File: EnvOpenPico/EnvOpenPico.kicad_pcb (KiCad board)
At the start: 2 copper layers, 21.5 x 51.3 mm, 57 parts, among them J2 SKRKAEE020, J3 2.54mm header 01x20, J4 2.54mm header 01x20, J5 Conn_01x03_Male, U1 TLV75533PDBVR, U3 RP2040, Y1 3225_4P

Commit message: dont remember what I changed but commit for safety
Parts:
- removed kibuzzard-628ADE15: G***, kibuzzard-628ADE15

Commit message: updated readme
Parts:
- removed kibuzzard-628939D8: G***, kibuzzard-628939D8
- removed kibuzzard-628939E9: G***, kibuzzard-628939E9
- removed kibuzzard-62893A77: G***, kibuzzard-62893A77
- removed kibuzzard-628A86BE: G***, kibuzzard-628A86BE
- FLASH1: value ZD25WQ16BUIGR -> w25q16jvuxiq
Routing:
- net GND: track 33.5 -> 31.8 mm
- net /RUN: track 14.1 -> 15.0 mm

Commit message: faff and things, no important changes.
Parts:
- removed kibuzzard-628A892C: G***, kibuzzard-628A892C
- FLASH1: value w25q16jvuxiq -> W25Q16JV
- U1: value TLV75533PDBVR -> TLV75733PDBVR
- moved C15 1.41 mm to (98.2, 80.2), turned to 90 degrees
- moved R1 1.02 mm to (100.6, 75.0)
- moved R2 0.88 mm to (98.8, 75.1)
- moved C5 0.38 mm to (98.8, 76.1)
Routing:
- net GND: track 31.8 -> 33.8 mm
- net /~{USB_BOOT}: track 5.99 -> 4.95 mm
- net /RUN: track 15.0 -> 14.4 mm
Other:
- board text added: "BOOT"

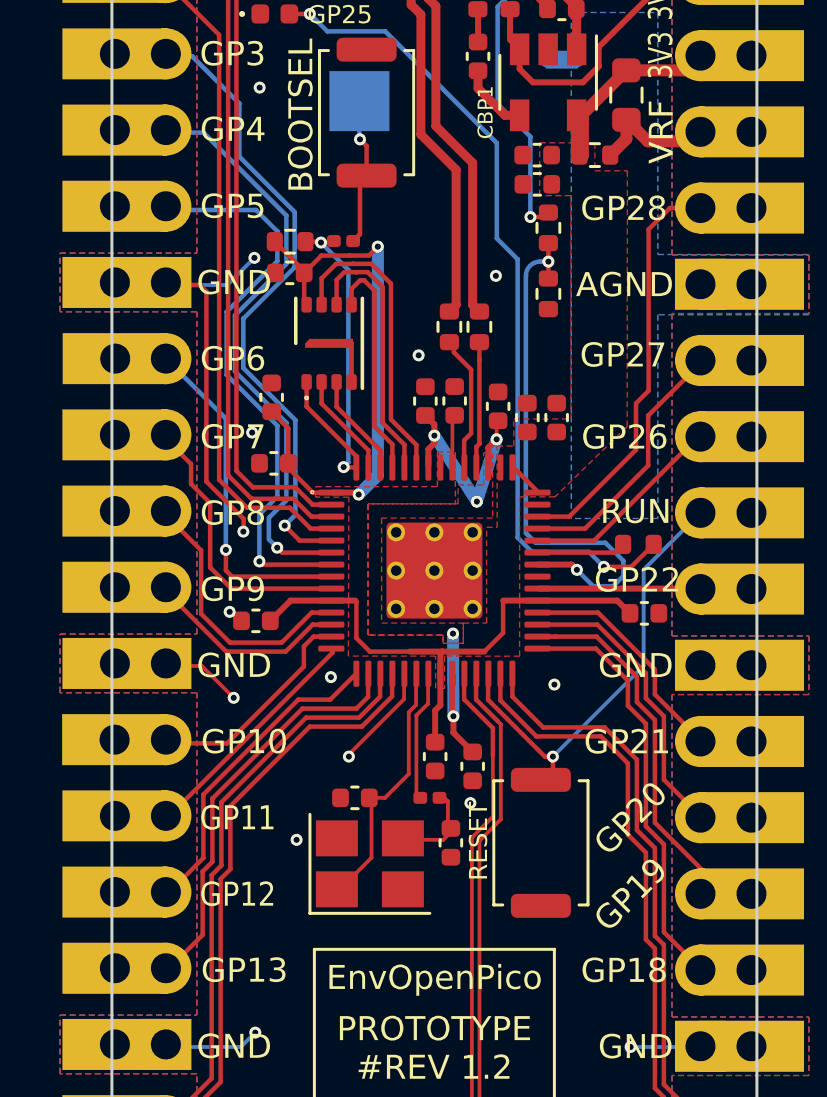
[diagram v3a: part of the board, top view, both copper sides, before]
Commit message: lots of changes, swapped many parts to 0402, swapped SOT regulator to small WSON, made sure there is proper parity between footprint and value, etc etc etc
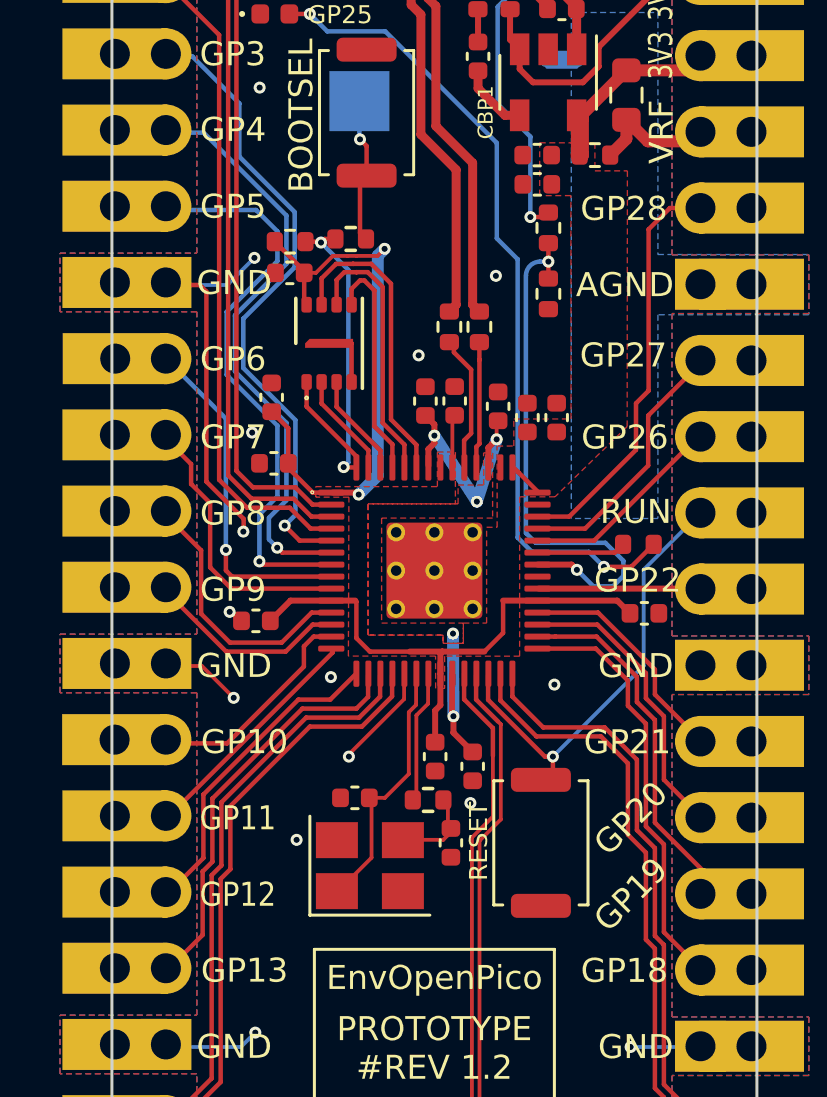
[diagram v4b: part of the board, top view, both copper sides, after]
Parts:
- R1, R11: value 1K 0201 -> 1K 0402; footprint Resistor_SMD:R_0201_0603Metric -> Resistor_SMD:R_0402_1005Metric
- moved R1 0.25 mm to (100.9, 75.0)
- moved R11 0.09 mm to (103.4, 93.7)
- moved Y1 0.06 mm to (101.5, 95.9)

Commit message: made some smaller components generated new gerber
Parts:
- J2, RSW1: value SKRKAEE020 -> TSA343G00-250J2
- moved RSW1 0.66 mm to (107.1, 95.8)
- moved C16 0.57 mm to (107.9, 80.4)
- moved C10 0.55 mm to (106.8, 80.4)
- moved C3 0.17 mm to (105.8, 80.4)
- moved GPIO25_LED1 0.16 mm to (98.3, 67.3)
- moved J2 0.12 mm to (101.5, 70.7)
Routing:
- net /RUN: track 14.4 -> 15.8 mm
- net /~{USB_BOOT}: track 4.87 -> 5.92 mm
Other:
- board text added: "25"
- board text removed: "GP25"

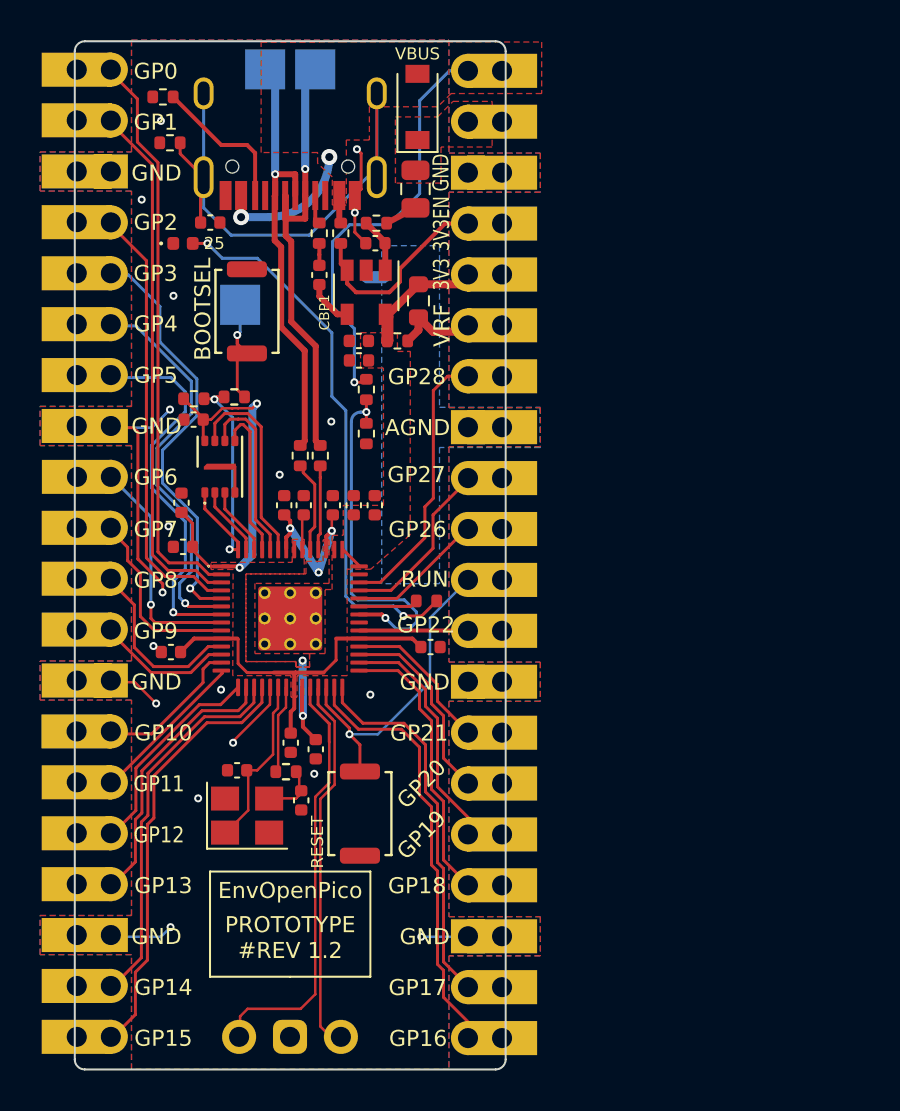
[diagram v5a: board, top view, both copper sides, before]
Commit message: swapped flash for one that was in stock.
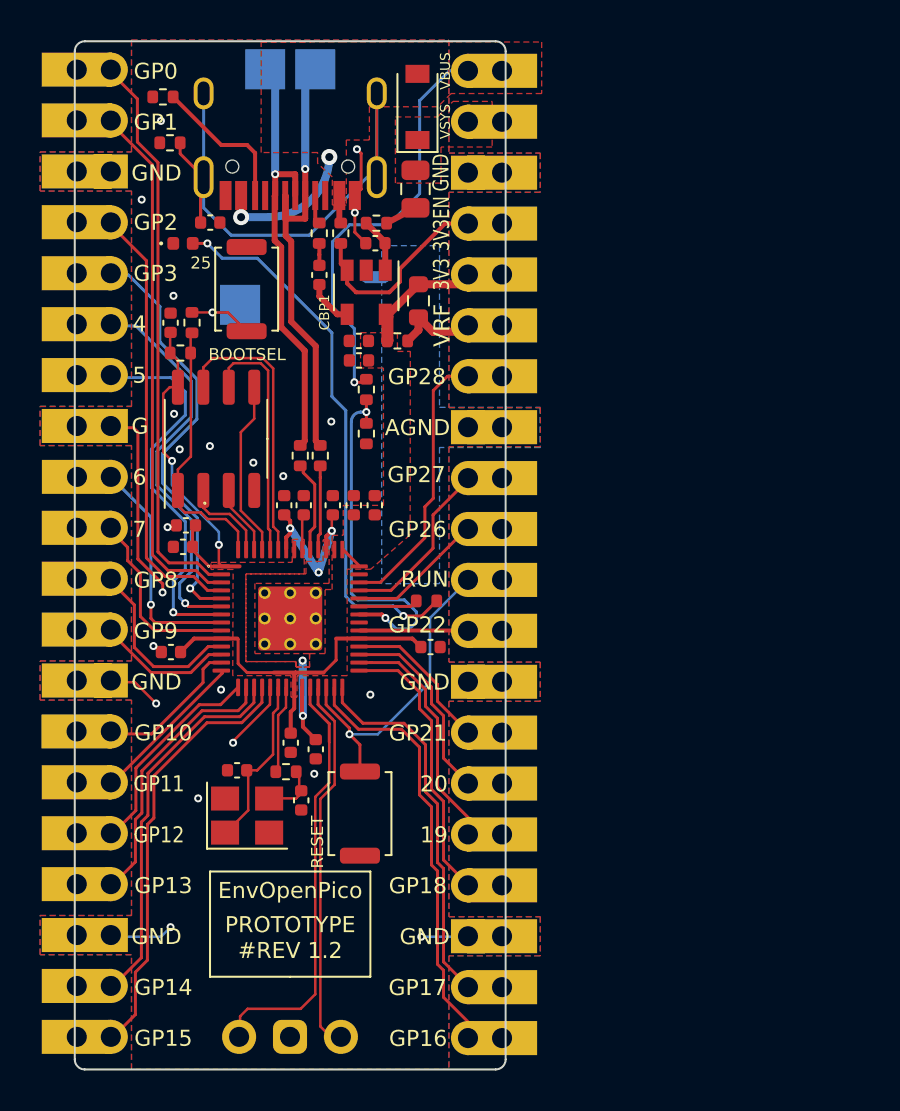
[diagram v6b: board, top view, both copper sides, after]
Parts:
- FLASH1: value W25Q16JV -> W25Q16JVSNIQ; footprint Package_SON:SON-8-1EP_3x2mm_P0.5mm_EP1.4x1.6mm -> Package_SO:SO-8_3.9x4.9mm_P1.27mm
- moved C5 4.97 mm to (97.7, 71.3), turned to 90 degrees
- moved R1 4.27 mm to (98.7, 71.3), turned to 90 degrees
- moved R2 2.38 mm to (98.2, 72.8)
- moved FLASH1 1.40 mm to (100.0, 77.1)
- moved C15 1.15 mm to (98.4, 81.4), turned to 180 degrees
- moved J2 1.11 mm to (101.5, 69.6)
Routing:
- net GND: track 33.8 -> 28.5 mm, vias 19 -> 22
- net /QSPI_SD3: track 10.1 -> 14.0 mm
- net /QSPI_SCLK: track 8.99 -> 12.1 mm
- net +3V3: track 47.0 -> 45.7 mm
- net /~{USB_BOOT}: track 5.92 -> 4.65 mm
- net /QSPI_SD0: track 7.69 -> 8.82 mm
- net /QSPI_SD1: track 3.50 -> 4.42 mm
- net /QSPI_SS: track 12.9 -> 13.4 mm, vias 2 -> 0
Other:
- board text added: "19"
- board text added: "20"
- board text added: "4"
- board text added: "5"
- board text added: "6"
- board text added: "7"
- board text added: "G"

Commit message: various updates including README
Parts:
- R3, R4: value 27 0402 -> 27r 0402 resistor
- U1: value TLV75733PDBVR -> SOT-23-5 5.5V 3.3V 500mA
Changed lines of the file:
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@@
       (effects (font (size 1 1) (thickness 0.15)))
     )
-    (fp_text value "27 0402" (at 0 1.17 90) (layer "F.Fab")
+    (fp_text value "27r 0402 resistor" (at 0 1.17 90) (layer "F.Fab")
       (effects (font (size 1 1) (thickness 0.15)))
     )
@@
       (effects (font (size 1 1) (thickness 0.15)))
     )
-    (fp_text value "27 0402" (at 0 1.17 90) (layer "F.Fab")
+    (fp_text value "27r 0402 resistor" (at 0 1.17 90) (layer "F.Fab")
       (effects (font (size 1 1) (thickness 0.15)))
     )
@@
       (effects (font (size 1 1) (thickness 0.15)))
     )
-    (fp_text value "TLV75733PDBVR" (at 0 2.9 90) (layer "F.Fab")
-      (effects (font (size 1 1) (thickness 0.15)))
-    )
+    (fp_text value "SOT-23-5 5.5V 3.3V 500mA" (at 0 2.9 90) (layer "F.Fab")
+      (effects (font (size 1 1) (thickness 0.15)))
+    )

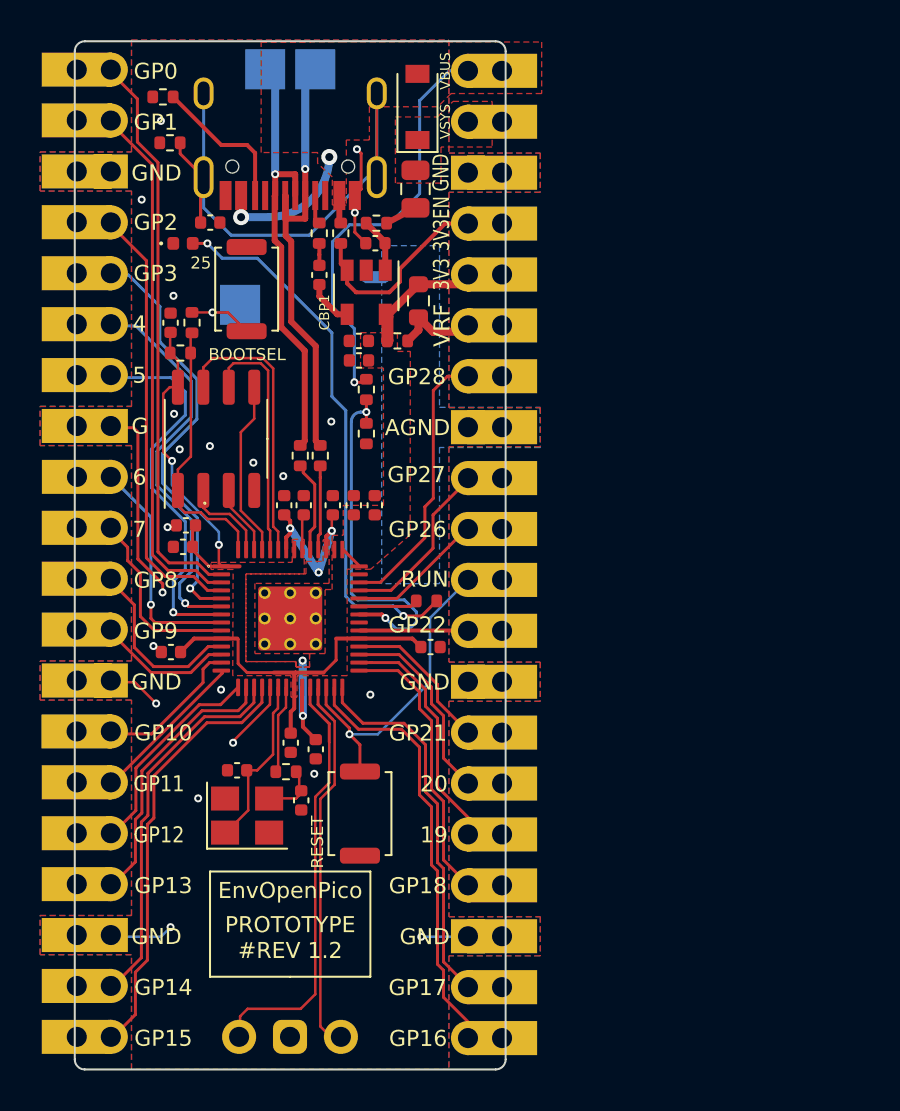
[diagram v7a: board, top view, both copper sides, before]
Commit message: incr version, added mosfet and led for GP23, marked GP24, tiny bits of cleanup and DRC checks.
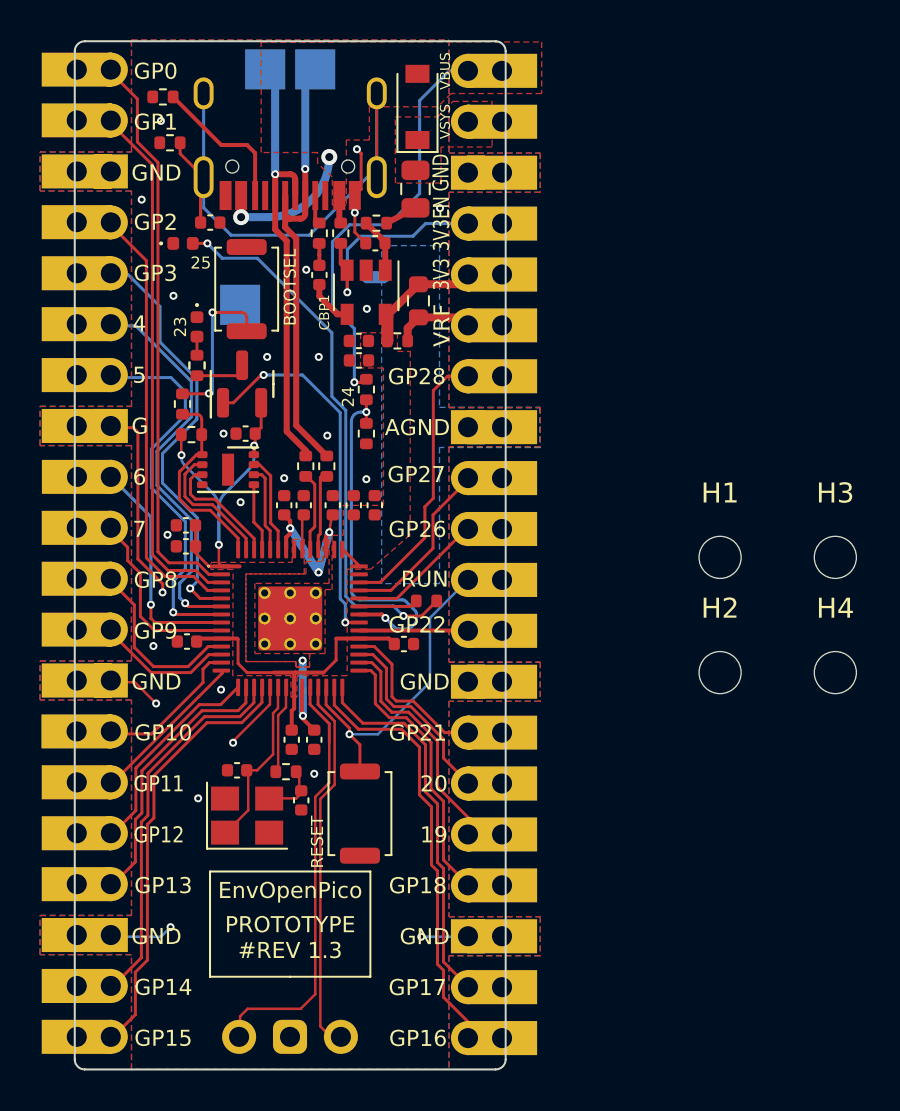
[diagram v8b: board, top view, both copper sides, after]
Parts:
- added GP23_LED1: GP23 LED_0402, LED_SMD:LED_0402_1005Metric, F.Cu at (99.0, 71.5)
- added GPIO24_RESISTOR1: 1K 0402, Resistor_SMD:R_0402_1005Metric, F.Cu at (99.0, 73.4)
- added H1: MountingHole, MountingHole:MountingHole_2.1mm, F.Cu at (125.1, 83.0)
- added H2: MountingHole, MountingHole:MountingHole_2.1mm, F.Cu at (125.1, 88.7)
- added H3: MountingHole, MountingHole:MountingHole_2.1mm, F.Cu at (130.8, 83.0)
- added H4: MountingHole, MountingHole:MountingHole_2.1mm, F.Cu at (130.8, 88.7)
- added Q1: SI2301B, Package_TO_SOT_SMD:SOT-23, F.Cu at (101.2, 74.3)
- FLASH1: value W25Q16JVSNIQ -> W25Q16JVUXIQ; footprint Package_SO:SO-8_3.9x4.9mm_P1.27mm -> Package_SON:SON-8-1EP_3x2mm_P0.5mm_EP1.4x1.6mm
- R102: value 1M 0402 -> 220 0402
- moved C5 6.68 mm to (101.4, 76.8), turned to 180 degrees
- moved R2 4.11 mm to (98.7, 76.8)
- moved R1 4.09 mm to (98.3, 75.3)
- moved FLASH1 1.65 mm to (100.5, 78.6), turned to 0 degrees
- moved C13 1.33 mm to (109.3, 87.3)
- moved C18 0.96 mm to (98.5, 87.2)
- moved R4 0.62 mm to (105.5, 78.4)
- moved R3 0.59 mm to (104.4, 78.4)
- moved C6 0.48 mm to (104.8, 92.1)
- moved C14 0.16 mm to (103.7, 92.1)
- moved C11 0.15 mm to (98.5, 82.4)
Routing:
- net /GPIO23: track 0.00 -> 18.5 mm, vias 0 -> 2
- net /QSPI_SD3: track 14.0 -> 4.96 mm
- net /QSPI_SCLK: track 12.1 -> 4.30 mm
- net /QSPI_SD0: track 8.82 -> 3.41 mm
- net /~{USB_BOOT}: track 4.65 -> 9.61 mm, vias 1 -> 2
- net /QSPI_SS: track 13.4 -> 10.0 mm
- net Net-(GPIO24_RESISTOR1-Pad2): track 0.00 -> 2.77 mm
- net /QSPI_SD2: track 3.48 -> 6.07 mm
- net /QSPI_SD1: track 4.42 -> 6.66 mm
- net 3V3_EN: track 9.67 -> 11.3 mm, vias 0 -> 1
- net Net-(GP23_LED1-Pad2): track 0.00 -> 0.93 mm
- net +1V1: track 14.2 -> 13.5 mm
- net +3V3: track 45.7 -> 45.1 mm, vias 2 -> 3
- net GND: vias 22 -> 25
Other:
- board text added: "23"
- board text added: "24"
- board text added: "PROTOTYPE #REV 1.3"
- board text removed: "PROTOTYPE #REV 1.2"
